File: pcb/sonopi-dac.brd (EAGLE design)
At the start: 65 x 30 mm, 24 parts, among them J1 AV2-8.4-10GA, U1 PCM5122PW, U2 MCP1703AT-3302E/CB, X1 RASPI_BOARD_B+#_ZERO, X2 22.5792MHz, X3 24.576MHz

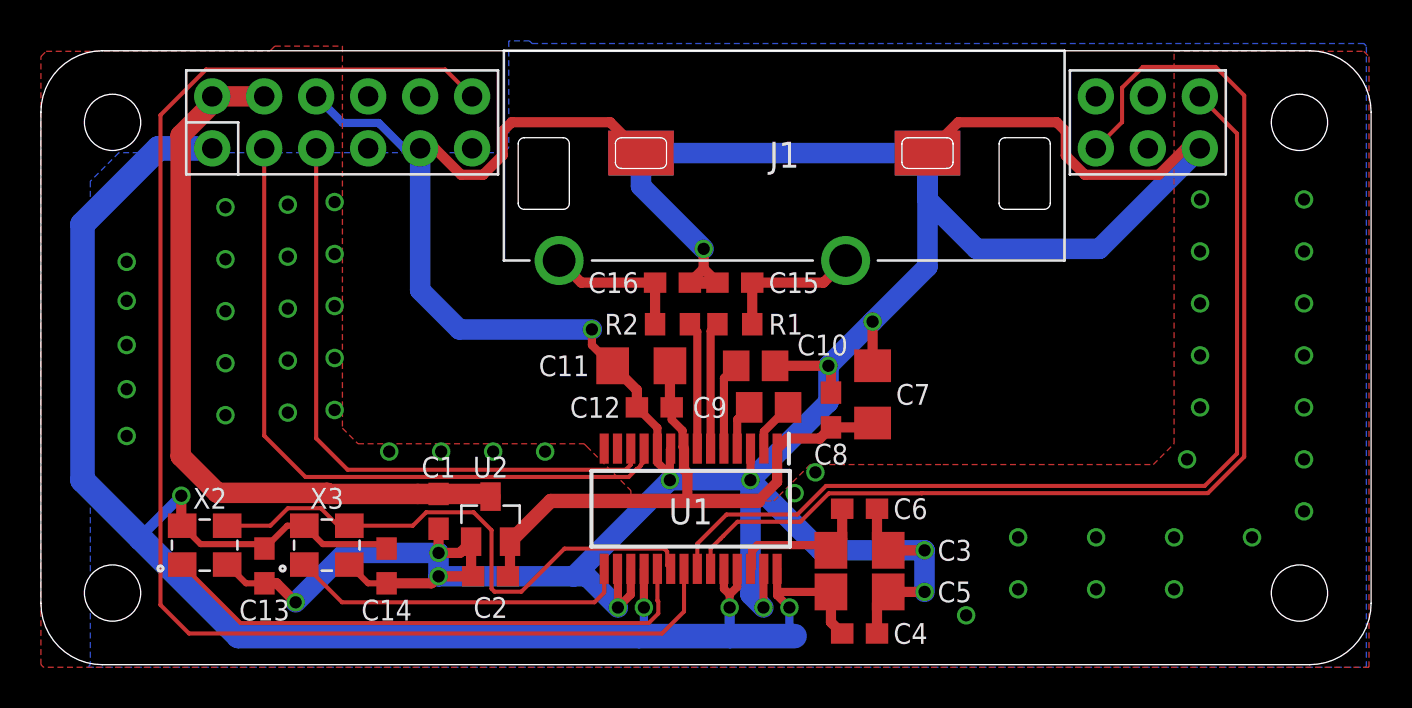
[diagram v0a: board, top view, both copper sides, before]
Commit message: add artwork design
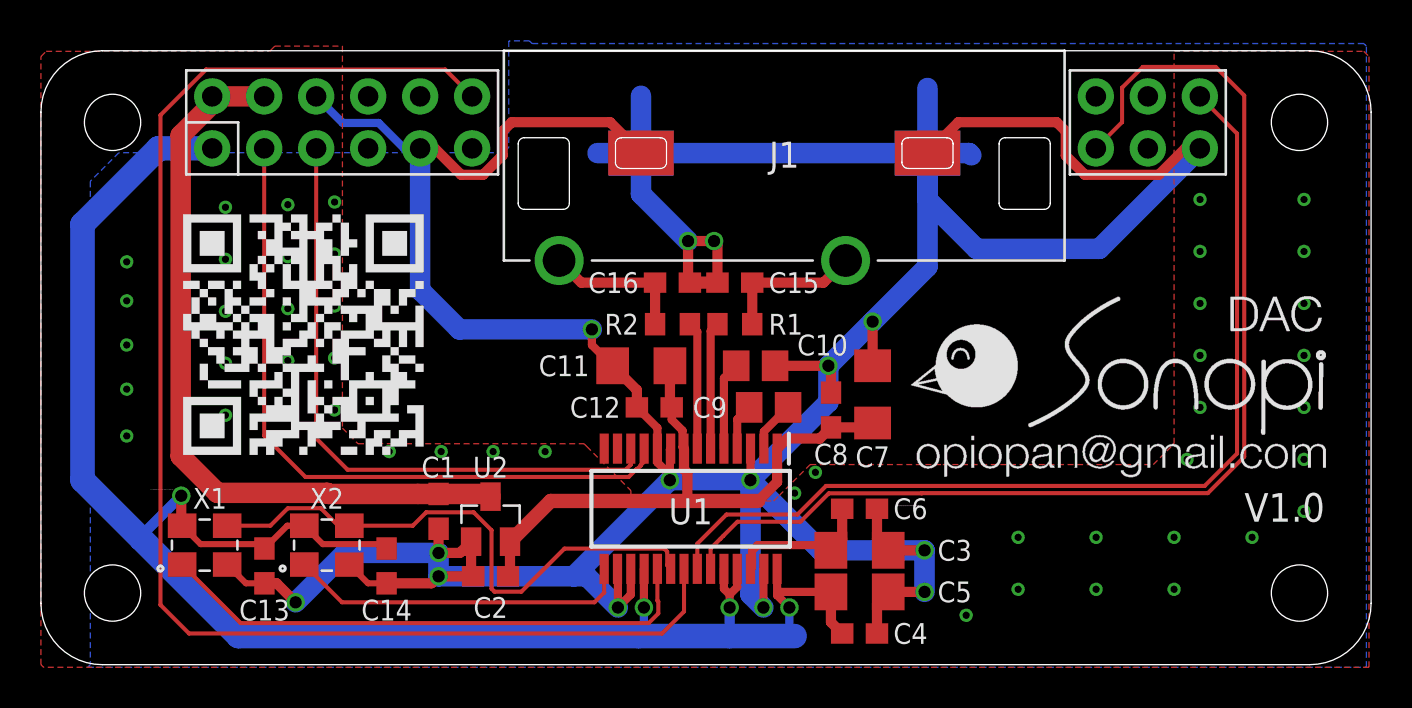
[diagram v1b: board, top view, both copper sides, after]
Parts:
- removed X3: 24.576MHz, oscillator:3225-SMD
- added J2: RASPI_BOARD_B+#_ZERO, raspi-zero-i2s:RASPI_BOARD_B+HAT_ZERO
- added U$1: (no value), logo:SONOPI-DAC-LOGO
- added U$2: (no value), logo:SONOPI-DAC-QRCODE
- X1: value RASPI_BOARD_B+#_ZERO -> 22.5792MHz; device raspi-zero-i2s:RASPI_BOARD_B+HAT_ZERO -> oscillator:3225-SMD
- X2: value 22.5792MHz -> 24.576MHz
- moved X1 9.91 mm to (8.00, 5.84)
- moved X2 5.97 mm to (14.0, 5.84)
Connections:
- net +3V3: now also J2.1, X1.4; no longer X1.1, X3.4
- net +5V: now also J2.2, J2.4; no longer X1.2, X1.4
- net BCLK: now also J2.12; no longer X1.12
- net DATA: now also J2.40; no longer X1.40
- net EN41: now also X1.1; no longer X2.1
- net EN48: now also X2.1; no longer X3.1
- net GND: now also J2.39, J2.6, J2.9, X1.2; no longer X1.39, X1.6, X1.9, X3.2
- net LRCLK: now also J2.35; no longer X1.35
- net SCL: now also J2.5; no longer X1.5
- net SCLK: now also X1.3; no longer X3.3
- net SDA: now also J2.3; no longer X1.3
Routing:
- net GND: track 209.4 -> 221.8 mm, vias 60 -> 61
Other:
- board text added: "V1.0"

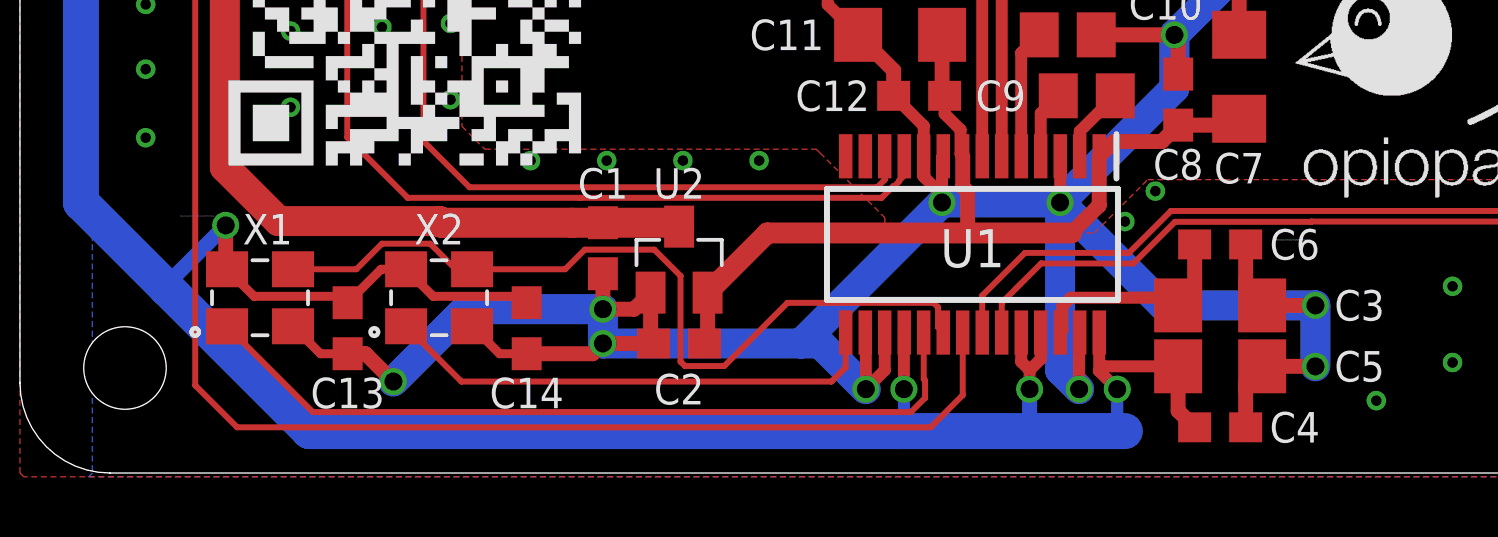
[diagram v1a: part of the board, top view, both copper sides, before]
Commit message: fix minor probrems, and add scripts to generate decal image for 3D rendering
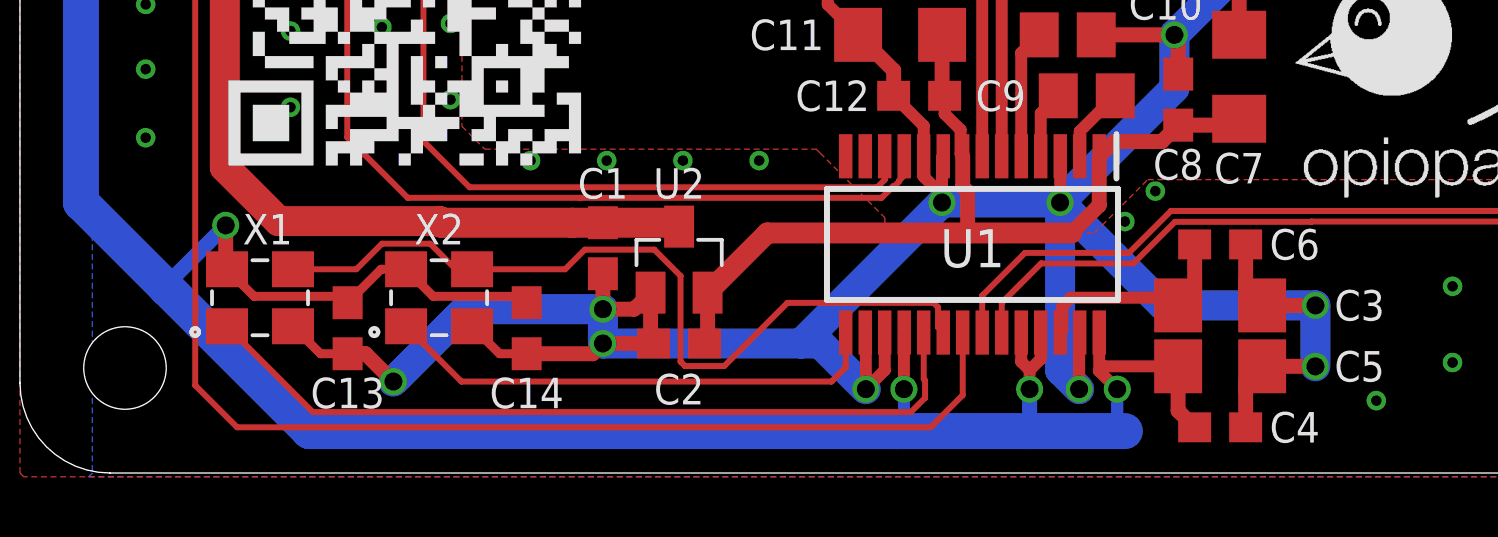
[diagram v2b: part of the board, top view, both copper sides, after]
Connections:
- net EN41 renamed EN44
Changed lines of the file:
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@@
 </layers>
 <board>
-<fusionsync huburn="a.cGVyc29uYWw6dWUyYmE2M2My" projecturn="a.cGVyc29uYWw6dWUyYmE2M2MyIzIwMTgwOTE3MTQ5MTY5Mjgx" f3durn="urn:adsk.wipprod:dm.lineage:frYCqByTTnG5slPWVEB-oA" pcbguid="7cebb721-e281-4a90-b6c0-b829a01244c8" lastpulledtime="" lastsyncedchangeguid="4c299219-e58e-1293-3d57-04ebac70f302"/>
+<fusionsync huburn="a.cGVyc29uYWw6dWUyYmE2M2My" projecturn="a.cGVyc29uYWw6dWUyYmE2M2MyIzIwMTgwOTE3MTQ5MTY5Mjgx" f3durn="urn:adsk.wipprod:dm.lineage:frYCqByTTnG5slPWVEB-oA" pcbguid="7cebb721-e281-4a90-b6c0-b829a01244c8" lastpulledtime="" lastsyncedchangeguid="46c38bd1-cc02-f853-66d1-19df69127135"/>
 <plain>
 <text x="62.738" y="6.985" size="1.4" layer="21" align="bottom-right">V1.0</text>
@@
 <attribute name="VALUE" x="30.607" y="14.478" size="1.27" layer="27" rot="R180"/>
 </element>
-<element name="U$1" library="logo" library_urn="urn:adsk.eagle:library:5477443" package="SONOPI-DAC-LOGO" override_package3d_urn="urn:adsk.eagle:package:15331970/2" override_package_urn="urn:adsk.eagle:footprint:15331971/1" value="" x="41.783" y="7.874" smashed="yes"/>
-<element name="U$2" library="logo" library_urn="urn:adsk.eagle:library:5477443" package="SONOPI-DAC-QRCODE" override_package3d_urn="urn:adsk.eagle:package:15331985/2" override_package_urn="urn:adsk.eagle:footprint:15331986/1" value="" x="5.334" y="8.636" smashed="yes"/>
+<element name="U$1" library="logo" library_urn="urn:adsk.eagle:library:5477443" package="SONOPI-DAC-LOGO" override_package3d_urn="urn:adsk.eagle:package:15331970/2" override_package_urn="urn:adsk.eagle:footprint:15331971/1" override_locally_modified="yes" value="" x="41.783" y="7.874" smashed="yes"/>
+<element name="U$2" library="logo" library_urn="urn:adsk.eagle:library:5477443" package="SONOPI-DAC-QRCODE" override_package3d_urn="urn:adsk.eagle:package:15331985/2" override_package_urn="urn:adsk.eagle:footprint:15331986/1" override_locally_modified="yes" value="" x="5.334" y="8.636" smashed="yes"/>
 </elements>
 <signals>
@@
 <wire x1="23.47555" y1="3.5656" x2="25.58185" y2="5.6719" width="0.2" layer="1"/>
 </signal>
-<signal name="EN41">
-<contactref element="U1" pad="19"/>
-<contactref element="X1" pad="1"/>
-<wire x1="30.1688" y1="3.08594375" x2="30.1688" y2="2.50205625" width="0.2" layer="1"/>
-<wire x1="30.1688" y1="2.50205625" x2="29.69874375" y2="2.032" width="0.2" layer="1"/>
-<wire x1="30.125" y1="4.682" x2="30.125" y2="3.12974375" width="0.2" layer="1"/>
-<wire x1="30.125" y1="3.12974375" x2="30.1688" y2="3.08594375" width="0.2" layer="1"/>
-<wire x1="29.69874375" y1="2.032" x2="9.761" y2="2.032" width="0.2" layer="1"/>
-<wire x1="9.761" y1="2.032" x2="6.901" y2="4.892" width="0.2" layer="1"/>
-</signal>
 <signal name="EN48">
 <contactref element="U1" pad="15"/>
@@
 <wire x1="30.011" y1="18.669" x2="30.011" y2="16.637" width="0.5" layer="1"/>
 </signal>
+<signal name="EN44">
+<contactref element="X1" pad="1"/>
+<contactref element="U1" pad="19"/>
+<wire x1="30.1688" y1="3.08594375" x2="30.1688" y2="2.50205625" width="0.2" layer="1"/>
+<wire x1="30.1688" y1="2.50205625" x2="29.69874375" y2="2.032" width="0.2" layer="1"/>
+<wire x1="30.125" y1="4.682" x2="30.125" y2="3.12974375" width="0.2" layer="1"/>
+<wire x1="30.125" y1="3.12974375" x2="30.1688" y2="3.08594375" width="0.2" layer="1"/>
+<wire x1="9.761" y1="2.032" x2="29.69874375" y2="2.032" width="0.2" layer="1"/>
+<wire x1="6.901" y1="4.892" x2="9.761" y2="2.032" width="0.2" layer="1"/>
+</signal>
 </signals>
